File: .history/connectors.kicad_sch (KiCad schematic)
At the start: 4 parts, among them J1 Conn_01x04_Pin, J2 Conn_01x04_Pin, J3 Conn_01x09_Pin, J4 Conn_02x03_Odd_Even

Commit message: footprint assigned
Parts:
- J1, J2: footprint (none) -> Connector_PinHeader_2.54mm:PinHeader_1x04_P2.54mm_Vertical
- J3: footprint (none) -> Connector_PinHeader_2.54mm:PinHeader_1x09_P2.54mm_Vertical
- J4: footprint (none) -> Connector_PinHeader_2.54mm:PinHeader_2x03_P2.54mm_Vertical
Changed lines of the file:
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@@
 			)
 		)
-		(property "Footprint" ""
+		(property "Footprint" "Connector_PinHeader_2.54mm:PinHeader_1x09_P2.54mm_Vertical"
 			(at 77.47 83.82 0)
 			(hide yes)
@@
 			)
 		)
-		(property "Footprint" ""
+		(property "Footprint" "Connector_PinHeader_2.54mm:PinHeader_1x04_P2.54mm_Vertical"
 			(at 77.47 54.61 0)
 			(hide yes)
@@
 			)
 		)
-		(property "Footprint" ""
+		(property "Footprint" "Connector_PinHeader_2.54mm:PinHeader_1x04_P2.54mm_Vertical"
 			(at 97.79 54.61 0)
 			(hide yes)
@@
 			)
 		)
-		(property "Footprint" ""
+		(property "Footprint" "Connector_PinHeader_2.54mm:PinHeader_2x03_P2.54mm_Vertical"
 			(at 100.33 77.47 0)
 			(hide yes)

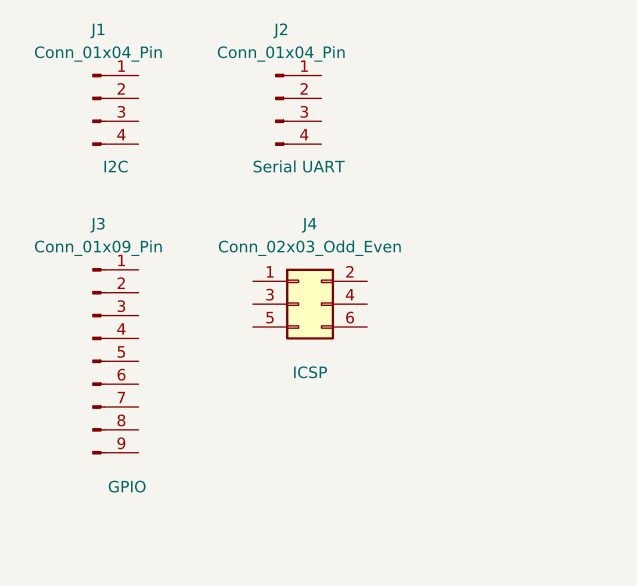
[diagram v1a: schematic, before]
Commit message: wiring in 2nd sheet done
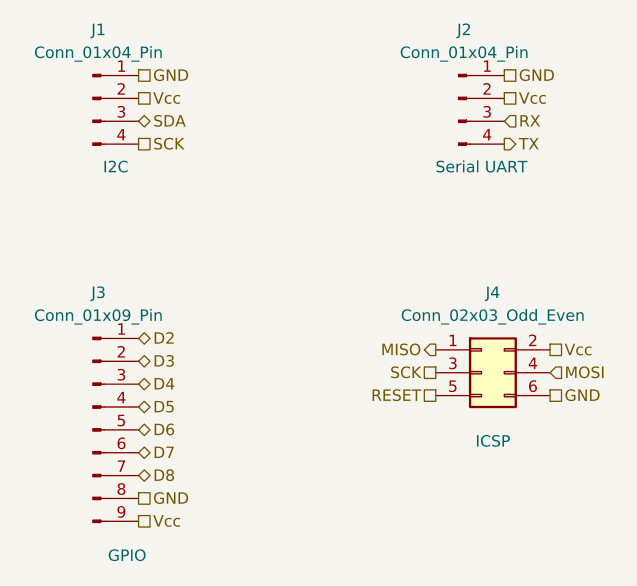
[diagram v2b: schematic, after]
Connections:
- net D2: now reaches J3.1 (Pin_1)
- net D3: now reaches J3.2 (Pin_2)
- net D4: now reaches J3.3 (Pin_3)
- net D5: now reaches J3.4 (Pin_4)
- net D6: now reaches J3.5 (Pin_5)
- net D7: now reaches J3.6 (Pin_6)
- net D8: now reaches J3.7 (Pin_7)
- net GND: now reaches J3.8 (Pin_8)
- net GND: now also J1.1 (Pin_1), J2.1 (Pin_1), J4.6 (Pin_6)
- net Vcc: now reaches J3.9 (Pin_9)
- net Vcc: now also J1.2 (Pin_2), J2.2 (Pin_2), J4.2 (Pin_2)
- net SDA: now reaches J1.3 (Pin_3)
- net SCK: now reaches J1.4 (Pin_4)
- net SCK: now also J4.3 (Pin_3)
- net RX: now reaches J2.3 (Pin_3)
- net TX: now reaches J2.4 (Pin_4)
- net MISO: now reaches J4.1 (Pin_1)
- net MOSI: now reaches J4.4 (Pin_4)
- net RESET: now reaches J4.5 (Pin_5)
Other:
- moved on the sheet: J2, J3, J4
